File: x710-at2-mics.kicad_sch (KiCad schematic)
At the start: 85 parts, among them U10 74LVC1G07_SOT-753, U7 NTS0102_TSSOP, U8 NTS0102_TSSOP, U9 EZX710AT2_S_LMR5, Y2 Resonator_50MHz_XRCGE

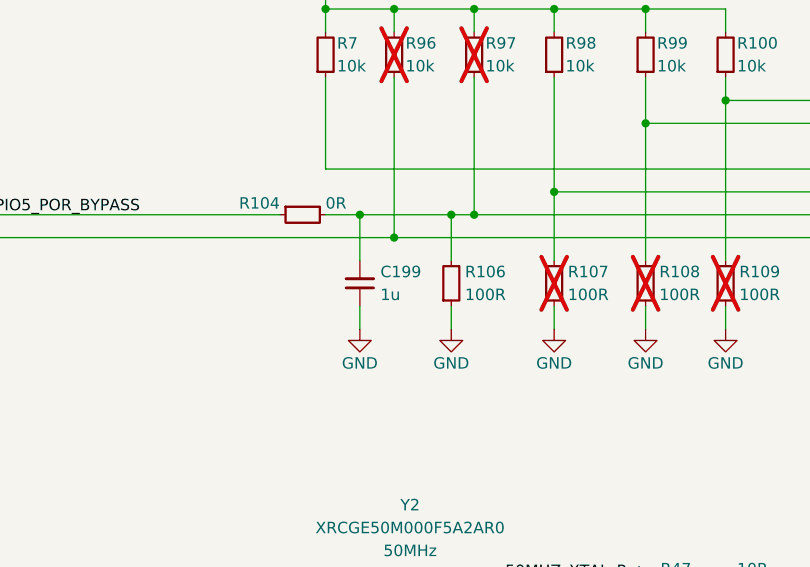
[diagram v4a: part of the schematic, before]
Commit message: [#86351] WIP: Layout flash memory
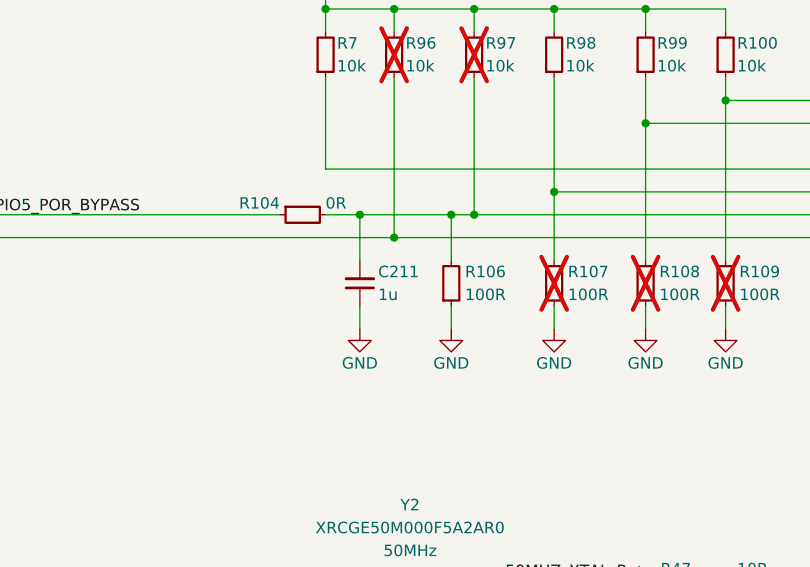
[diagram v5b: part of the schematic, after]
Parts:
- removed C199: C_1u_16V_X7R_0603, antmicro-footprints:C_0603_1608Metric, symbol antmicroCapacitors0603:C_1u_16V_X7R_0603
- added C211: C_1u_25V_0402, antmicro-footprints:C_0402_1005Metric, symbol antmicroCapacitors0402:C_1u_25V_0402
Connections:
- net GND: now also C211.1
- net POR_BYPASS: now also C211.2
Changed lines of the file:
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@@
-	)
-	(symbol
-		(lib_id "antmicroCapacitors0603:C_1u_16V_X7R_0603")
-		(at 114.3 129.54 90)
-		(unit 1)
-		(exclude_from_sim no)
-		(in_bom yes)
-		(on_board yes)
-		(dnp no)
-		(property "Reference" "C199"
-			(at 116.586 125.73 90)
-			(effects
-				(font
-					(size 1.27 1.27)
-					(thickness 0.15)
-				)
-				(justify right)
-			)
-		)
-		(property "Value" "C_1u_16V_X7R_0603"
-			(at 124.46 114.3 0)
-			(effects
-				(font
-					(size 1.27 1.27)
-					(thickness 0.15)
-				)
-				(justify left bottom)
-				(hide yes)
-			)
-		)
-		(property "Footprint" "antmicro-footprints:C_0603_1608Metric"
-			(at 127 114.3 0)
-			(effects
-				(font
-					(size 1.27 1.27)
-					(thickness 0.15)
-				)
-				(justify left bottom)
-				(hide yes)
-			)
-		)
-		(property "Datasheet" "https://www.kemet.com/en/us/capacitors/product/C0603C105K4RAC7411.html"
-			(at 129.54 114.3 0)
-			(effects
-				(font
-					(size 1.27 1.27)
-					(thickness 0.15)
-				)
-				(justify left bottom)
-				(hide yes)
-			)
-		)
-		(property "Description" "SMD Multilayer Ceramic Capacitor, 1µF, 16V, 0603, ±10%, X7R"
-			(at 114.3 129.54 0)
-			(effects
-				(font
-					(size 1.27 1.27)
-				)
-				(hide yes)
-			)
-		)
-		(property "MPN" "C0603C105K4RAC7411"
-			(at 132.08 114.3 0)
-			(effects
-				(font
-					(size 1.27 1.27)
-					(thickness 0.15)
-				)
-				(justify left bottom)
-				(hide yes)
-			)
-		)
-		(property "Val" "1u"
-			(at 116.586 128.27 90)
-			(effects
-				(font
-					(size 1.27 1.27)
-					(thickness 0.15)
-				)
-				(justify right)
-			)
-		)
-		(property "Voltage" "16V"
-			(at 134.62 114.3 0)
-			(effects
-				(font
-					(size 1.27 1.27)
-					(thickness 0.15)
-				)
-				(justify left bottom)
-				(hide yes)
-			)
-		)
-		(property "Dielectric" "X7R"
-			(at 137.16 114.3 0)
-			(effects
-				(font
-					(size 1.27 1.27)
-					(thickness 0.15)
-				)
-				(justify left bottom)
-				(hide yes)
-			)
-		)
-		(property "Manufacturer" "KEMET"
-			(at 139.7 114.3 0)
-			(effects
-				(font
-					(size 1.27 1.27)
-					(thickness 0.15)
-				)
-				(justify left bottom)
-				(hide yes)
-			)
-		)
-		(property "License" "Apache-2.0"
-			(at 142.24 114.3 0)
-			(effects
-				(font
-					(size 1.27 1.27)
-					(thickness 0.15)
-				)
-				(justify left bottom)
-				(hide yes)
-			)
-		)
-		(property "Author" "Antmicro"
-			(at 144.78 114.3 0)
-			(effects
-				(font
-					(size 1.27 1.27)
-					(thickness 0.15)
-				)
-				(justify left bottom)
-				(hide yes)
-			)
-		)
-		(pin "1"
-		)
-		(pin "2"
-		)
-		(instances
-			(project ""
-				(path "/04bda987-e5eb-48b4-9e90-d8211dc11b39/d0402c84-6d4c-4559-b85a-0c9b588a21c5"
-					(reference "C199")
-					(unit 1)
-				)
-			)
-		)
 	)
 	(symbol
@@
 					(unit 1)
 				)
+			)
+		)
+	)
+	(symbol
+		(lib_id "antmicroCapacitors0402:C_1u_25V_0402")
+		(at 114.3 129.54 90)
+		(unit 1)
+		(exclude_from_sim no)
+		(in_bom yes)
+		(on_board yes)
+		(dnp no)
+		(property "Reference" "C211"
+			(at 116.332 125.73 90)
+			(effects
+				(font
+					(size 1.27 1.27)
+					(thickness 0.15)
+				)
+				(justify right)
+			)
+		)
+		(property "Value" "C_1u_25V_0402"
+			(at 124.46 109.22 0)
+			(effects
+				(font
+					(size 1.27 1.27)
+					(thickness 0.15)
+				)
+				(justify left bottom)
+				(hide yes)
+			)
+		)
+		(property "Footprint" "antmicro-footprints:C_0402_1005Metric"
+			(at 127 109.22 0)
+			(effects
+				(font
+					(size 1.27 1.27)
+					(thickness 0.15)
+				)
+				(justify left bottom)
+				(hide yes)
+			)
+		)
+		(property "Datasheet" "https://www.murata.com/products/productdetail?partno=GRM155R61E105KE11%23"
+			(at 129.54 109.22 0)
+			(effects
+				(font
+					(size 1.27 1.27)
+					(thickness 0.15)
+				)
+				(justify left bottom)
+				(hide yes)
+			)
+		)
+		(property "Description" "SMD Multilayer Ceramic Capacitor, 1 µF, 25 V, 0402 [1005 Metric], ± 10%, X5R, GRM Series"
+			(at 114.3 129.54 0)
+			(effects
+				(font
+					(size 1.27 1.27)
+				)
+				(hide yes)
+			)
+		)
+		(property "MPN" "GRM155R61E105KE11J"
+			(at 132.08 109.22 0)
+			(effects
+				(font
+					(size 1.27 1.27)
+					(thickness 0.15)
+				)
+				(justify left bottom)
+				(hide yes)
+			)
+		)
+		(property "Manufacturer" "Murata"
+			(at 134.62 109.22 0)
+			(effects
+				(font
+					(size 1.27 1.27)
+					(thickness 0.15)
+				)
+				(justify left bottom)
+				(hide yes)
+			)
+		)
+		(property "License" "Apache-2.0"
+			(at 137.16 109.22 0)
+			(effects
+				(font
+					(size 1.27 1.27)
+					(thickness 0.15)
+				)
+				(justify left bottom)
+				(hide yes)
+			)
+		)
+		(property "Author" "Antmicro"
+			(at 139.7 109.22 0)
+			(effects
+				(font
+					(size 1.27 1.27)
+					(thickness 0.15)
+				)
+				(justify left bottom)
+				(hide yes)
+			)
+		)
+		(property "Val" "1u"
+			(at 116.332 128.27 90)
+			(effects
+				(font
+					(size 1.27 1.27)
+					(thickness 0.15)
+				)
+				(justify right)
+			)
+		)
+		(property "Voltage" "25V"
+			(at 142.24 109.22 0)
+			(effects
+				(font
+					(size 1.27 1.27)
+				)
+				(justify left bottom)
+				(hide yes)
+			)
+		)
+		(property "Dielectric" "X5R"
+			(at 144.78 109.22 0)
+			(effects
+				(font
+					(size 1.27 1.27)
+				)
+				(justify left bottom)
+				(hide yes)
+			)
+		)
+		(pin "2"
+		)
+		(pin "1"
+		)
+		(instances
+			(project "oculink-to-10gbe-adapter"
+				(path "/04bda987-e5eb-48b4-9e90-d8211dc11b39/d0402c84-6d4c-4559-b85a-0c9b588a21c5"
+					(reference "C211")
+					(unit 1)
+				)

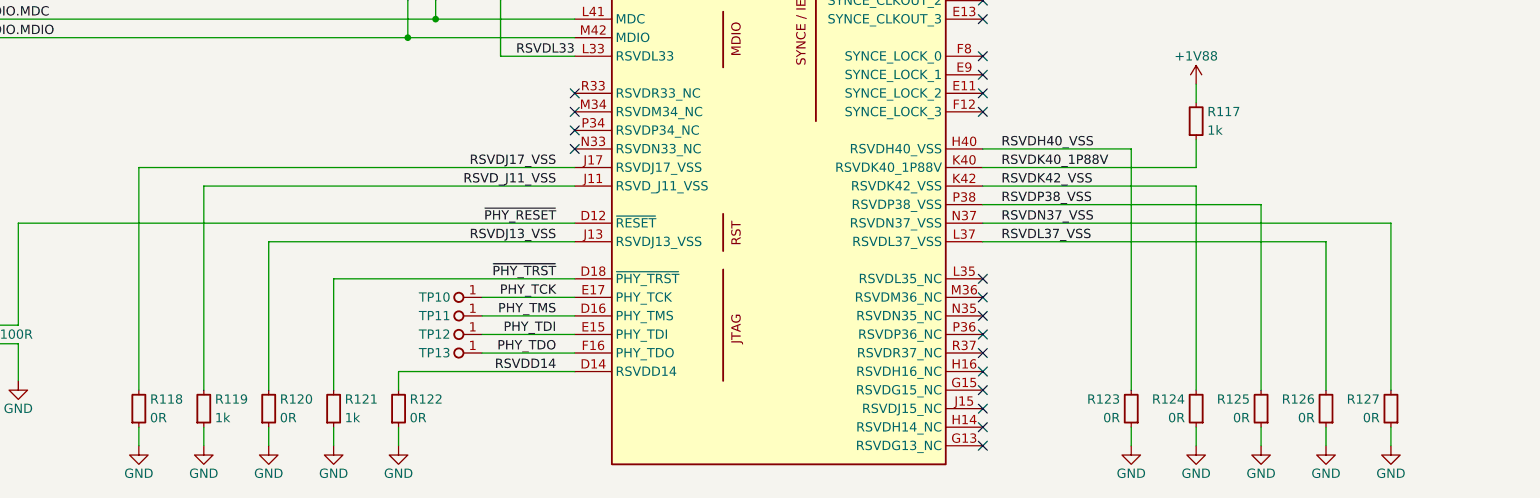
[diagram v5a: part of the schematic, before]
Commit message: [#86351] Replace RSVD_VSS 0Rs with direct connection
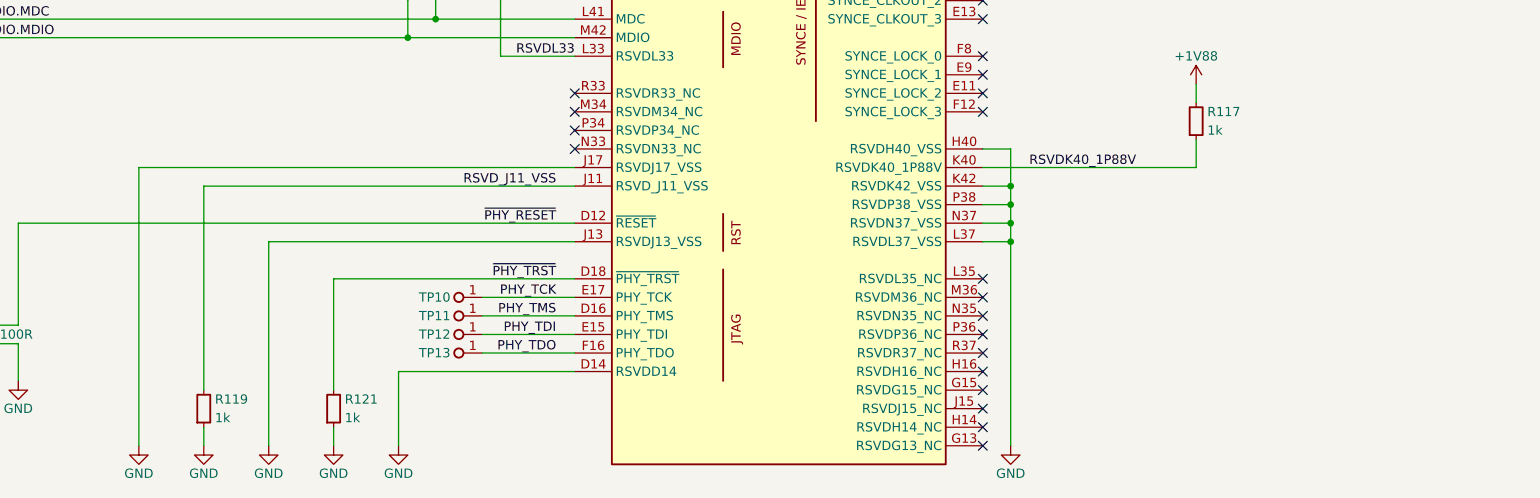
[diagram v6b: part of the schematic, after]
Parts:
- removed R118, R120, R122, R123, R124, R125, R126, R127: R_0R_0402, antmicro-footprints:R_0402_1005Metric, symbol antmicroResistors0402:R_0R_0402
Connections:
- net RSVDD14 is gone; now on net GND: U9.D14 (RSVDD14)
- net RSVDH40_VSS is gone; now on net GND: U9.H40 (RSVDH40_VSS)
- net RSVDJ13_VSS is gone; now on net GND: U9.J13 (RSVDJ13_VSS)
- net RSVDJ17_VSS is gone; now on net GND: U9.J17 (RSVDJ17_VSS)
- net RSVDK42_VSS is gone; now on net GND: U9.K42 (RSVDK42_VSS)
- net RSVDL37_VSS is gone; now on net GND: U9.L37 (RSVDL37_VSS)
- net RSVDN37_VSS is gone; now on net GND: U9.N37 (RSVDN37_VSS)
- net RSVDP38_VSS is gone; now on net GND: U9.P38 (RSVDP38_VSS)

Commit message: [#86351] Continue layout
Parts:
- removed R101, R95: R_0R_0402, antmicro-footprints:R_0402_1005Metric, symbol antmicroResistors0402:R_0R_0402
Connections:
- net SMBCLK is gone; now on net SMBus.SCL: R92.1, U9.R39 (SMBCLK)
- net SMBD is gone; now on net SMBus.SDA: R93.1, U9.T40 (SMBD)

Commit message: [#86351] Minor BOM consolidation
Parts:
- C198, C74, C75, C76, C77: value C_100n_16V_X7R_0402 -> C_100n_0402; symbol antmicroCapacitors0402:C_100n_16V_X7R_0402 -> antmicroCapacitors0402:C_100n_0402; Dielectric X7R -> X5R; MPN C0402C104J4RAC7411 -> GRM155R61H104KE14D; Manufacturer KEMET -> Murata; Voltage 16V -> 50V
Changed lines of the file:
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@@
 	)
 	(symbol
-		(lib_id "antmicroCapacitors0402:C_100n_16V_X7R_0402")
+		(lib_id "antmicroCapacitors0402:C_100n_0402")
 		(at 33.02 111.76 90)
 		(unit 1)
@@
 			)
 		)
-		(property "Value" "C_100n_16V_X7R_0402"
+		(property "Value" "C_100n_0402"
 			(at 55.88 96.52 0)
 			(effects
@@
 			)
 		)
-		(property "Datasheet" "https://www.kemet.com/en/us/capacitors/product/C0402C104J4RAC7411.html"
+		(property "Datasheet" "https://www.murata.com/products/productdetail?partno=GRM155R61H104KE14%23"
 			(at 60.96 96.52 0)
 			(effects
@@
 			)
 		)
-		(property "Description" "SMD Multilayer Ceramic Capacitor, 100nF, 50V, 0402, ±5%, X7R"
+		(property "Description" "SMD Multilayer Ceramic Capacitor, 0.1 µF, 50 V, 0402 [1005 Metric], ± 10%, X5R, GRM Series"
 			(at 33.02 111.76 0)
 			(effects
@@
 			)
 		)
-		(property "MPN" "C0402C104J4RAC7411"
+		(property "MPN" "GRM155R61H104KE14D"
 			(at 63.5 96.52 0)
 			(effects
@@
 			)
 		)
-		(property "Voltage" "16V"
+		(property "Voltage" "50V"
 			(at 43.18 96.52 0)
 			(effects
@@
 			)
 		)
-		(property "Dielectric" "X7R"
+		(property "Dielectric" "X5R"
 			(at 45.72 96.52 0)
 			(effects
@@
 			)
 		)
-		(property "Manufacturer" "KEMET"
+		(property "Manufacturer" "Murata"
 			(at 48.26 96.52 0)
 			(effects
@@
 	)
 	(symbol
-		(lib_id "antmicroCapacitors0402:C_100n_16V_X7R_0402")
+		(lib_id "antmicroCapacitors0402:C_100n_0402")
 		(at 97.79 179.07 90)
 		(unit 1)
@@
 			)
 		)
-		(property "Value" "C_100n_16V_X7R_0402"
+		(property "Value" "C_100n_0402"
 			(at 120.65 163.83 0)
 			(effects
@@
 			)
 		)
-		(property "Datasheet" "https://www.kemet.com/en/us/capacitors/product/C0402C104J4RAC7411.html"
+		(property "Datasheet" "https://www.murata.com/products/productdetail?partno=GRM155R61H104KE14%23"
 			(at 125.73 163.83 0)
 			(effects
@@
 			)
 		)
-		(property "Description" "SMD Multilayer Ceramic Capacitor, 100nF, 50V, 0402, ±5%, X7R"
+		(property "Description" "SMD Multilayer Ceramic Capacitor, 0.1 µF, 50 V, 0402 [1005 Metric], ± 10%, X5R, GRM Series"
 			(at 97.79 179.07 0)
 			(effects
@@
 			)
 		)
-		(property "MPN" "C0402C104J4RAC7411"
+		(property "MPN" "GRM155R61H104KE14D"
 			(at 128.27 163.83 0)
 			(effects
@@
 			)
 		)
-		(property "Voltage" "16V"
+		(property "Voltage" "50V"
 			(at 107.95 163.83 0)
 			(effects
@@
 			)
 		)
-		(property "Dielectric" "X7R"
+		(property "Dielectric" "X5R"
 			(at 110.49 163.83 0)
 			(effects
@@
 			)
 		)
-		(property "Manufacturer" "KEMET"
+		(property "Manufacturer" "Murata"
 			(at 113.03 163.83 0)
 			(effects
@@
 	)
 	(symbol
-		(lib_id "antmicroCapacitors0402:C_100n_16V_X7R_0402")
+		(lib_id "antmicroCapacitors0402:C_100n_0402")
 		(at 62.23 220.98 270)
 		(mirror x)
@@
 			)
 		)
-		(property "Value" "C_100n_16V_X7R_0402"
+		(property "Value" "C_100n_0402"
 			(at 39.37 205.74 0)
 			(effects
@@
 			)
 		)
-		(property "Datasheet" "https://www.kemet.com/en/us/capacitors/product/C0402C104J4RAC7411.html"
+		(property "Datasheet" "https://www.murata.com/products/productdetail?partno=GRM155R61H104KE14%23"
 			(at 34.29 205.74 0)
 			(effects
@@
 			)
 		)
-		(property "Description" "SMD Multilayer Ceramic Capacitor, 100nF, 50V, 0402, ±5%, X7R"
+		(property "Description" "SMD Multilayer Ceramic Capacitor, 0.1 µF, 50 V, 0402 [1005 Metric], ± 10%, X5R, GRM Series"
 			(at 62.23 220.98 0)
 			(effects
@@
 			)
 		)
-		(property "MPN" "C0402C104J4RAC7411"
+		(property "MPN" "GRM155R61H104KE14D"
 			(at 31.75 205.74 0)
 			(effects
@@
 			)
 		)
-		(property "Voltage" "16V"
+		(property "Voltage" "50V"
 			(at 52.07 205.74 0)
 			(effects
@@
 			)
 		)
-		(property "Dielectric" "X7R"
+		(property "Dielectric" "X5R"
 			(at 49.53 205.74 0)
 			(effects
@@
 			)
 		)
-		(property "Manufacturer" "KEMET"
+		(property "Manufacturer" "Murata"
 			(at 46.99 205.74 0)
 			(effects
@@
 	)
 	(symbol
-		(lib_id "antmicroCapacitors0402:C_100n_16V_X7R_0402")
+		(lib_id "antmicroCapacitors0402:C_100n_0402")
 		(at 97.79 220.98 90)
 		(unit 1)
@@
 			)
 		)
-		(property "Value" "C_100n_16V_X7R_0402"
+		(property "Value" "C_100n_0402"
 			(at 120.65 205.74 0)
 			(effects
@@
 			)
 		)
-		(property "Datasheet" "https://www.kemet.com/en/us/capacitors/product/C0402C104J4RAC7411.html"
+		(property "Datasheet" "https://www.murata.com/products/productdetail?partno=GRM155R61H104KE14%23"
 			(at 125.73 205.74 0)
 			(effects
@@
 			)
 		)
-		(property "Description" "SMD Multilayer Ceramic Capacitor, 100nF, 50V, 0402, ±5%, X7R"
+		(property "Description" "SMD Multilayer Ceramic Capacitor, 0.1 µF, 50 V, 0402 [1005 Metric], ± 10%, X5R, GRM Series"
 			(at 97.79 220.98 0)
 			(effects
@@
 			)
 		)
-		(property "MPN" "C0402C104J4RAC7411"
+		(property "MPN" "GRM155R61H104KE14D"
 			(at 128.27 205.74 0)
 			(effects
@@
 			)
 		)
-		(property "Voltage" "16V"
+		(property "Voltage" "50V"
 			(at 107.95 205.74 0)
 			(effects
@@
 			)
 		)
-		(property "Dielectric" "X7R"
+		(property "Dielectric" "X5R"
 			(at 110.49 205.74 0)
 			(effects
@@
 			)
 		)
-		(property "Manufacturer" "KEMET"
+		(property "Manufacturer" "Murata"
 			(at 113.03 205.74 0)
 			(effects
@@
 	)
 	(symbol
-		(lib_id "antmicroCapacitors0402:C_100n_16V_X7R_0402")
+		(lib_id "antmicroCapacitors0402:C_100n_0402")
 		(at 62.23 179.07 270)
 		(mirror x)
@@
 			)
 		)
-		(property "Value" "C_100n_16V_X7R_0402"
+		(property "Value" "C_100n_0402"
 			(at 39.37 163.83 0)
 			(effects
@@
 			)
 		)
-		(property "Datasheet" "https://www.kemet.com/en/us/capacitors/product/C0402C104J4RAC7411.html"
+		(property "Datasheet" "https://www.murata.com/products/productdetail?partno=GRM155R61H104KE14%23"
 			(at 34.29 163.83 0)
 			(effects
@@
 			)
 		)
-		(property "Description" "SMD Multilayer Ceramic Capacitor, 100nF, 50V, 0402, ±5%, X7R"
+		(property "Description" "SMD Multilayer Ceramic Capacitor, 0.1 µF, 50 V, 0402 [1005 Metric], ± 10%, X5R, GRM Series"
 			(at 62.23 179.07 0)
 			(effects
@@
 			)
 		)
-		(property "MPN" "C0402C104J4RAC7411"
+		(property "MPN" "GRM155R61H104KE14D"
 			(at 31.75 163.83 0)
 			(effects
@@
 			)
 		)
-		(property "Voltage" "16V"
+		(property "Voltage" "50V"
 			(at 52.07 163.83 0)
 			(effects
@@
 			)
 		)
-		(property "Dielectric" "X7R"
+		(property "Dielectric" "X5R"
 			(at 49.53 163.83 0)
 			(effects
@@
 			)
 		)
-		(property "Manufacturer" "KEMET"
+		(property "Manufacturer" "Murata"
 			(at 46.99 163.83 0)
 			(effects
